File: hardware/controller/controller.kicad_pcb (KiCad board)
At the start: 2 copper layers, 37 x 84 mm, 14 parts, among them J1 Conn_01x02_Pin, J2 Conn_01x02_Pin, J3 Conn_01x02_Pin, J4 Conn_01x02_Pin

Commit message: PCB routing checkpoint 1
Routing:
- net Net-(J1-Pin_2): track 0.00 -> 113.3 mm
- net Net-(J7-Pin_4): track 0.00 -> 75.4 mm
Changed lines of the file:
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@@
 		(layer "Edge.Cuts")
+	)
+	(segment
+		(start 151 62)
+		(end 151 63.5)
+		(width 0.2)
+		(layer "F.Cu")
+		(net 2)
+	)
+	(segment
+		(start 127.525 61.79)
+		(end 127.525 64.975)
+		(width 0.2)
+		(layer "F.Cu")
+		(net 2)
+	)
+	(segment
+		(start 149.525 61.79)
+		(end 147.9075 63.4075)
+		(width 0.2)
+		(layer "F.Cu")
+		(net 2)
+	)
+	(segment
+		(start 126 118.789)
+		(end 126 65)
+		(width 0.2)
+		(layer "F.Cu")
+		(net 2)
+	)
+	(segment
+		(start 127.525 64.975)
+		(end 127.5 65)
+		(width 0.2)
+		(layer "F.Cu")
+		(net 2)
+	)
+	(segment
+		(start 127.5 65)
+		(end 126 65)
+		(width 0.2)
+		(layer "F.Cu")
+		(net 2)
+	)
+	(segment
+		(start 151 63.5)
+		(end 148 63.5)
+		(width 0.2)
+		(layer "F.Cu")
+		(net 2)
+	)
+	(segment
+		(start 141.5 115)
+		(end 139.5 117)
+		(width 0.2)
+		(layer "F.Cu")
+		(net 2)
+	)
+	(segment
+		(start 127.2525 120.0415)
+		(end 126 118.789)
+		(width 0.2)
+		(layer "F.Cu")
+		(net 2)
+	)
+	(segment
+		(start 148 63.5)
+		(end 147.9075 63.4075)
+		(width 0.2)
+		(layer "F.Cu")
+		(net 2)
+	)
+	(segment
+		(start 154.5 61.5)
+		(end 151.5 61.5)
+		(width 0.2)
+		(layer "F.Cu")
+		(net 2)
+	)
+	(segment
+		(start 151.5 61.5)
+		(end 151 62)
+		(width 0.2)
+		(layer "F.Cu")
+		(net 2)
+	)
+	(segment
+		(start 126 65)
+		(end 122.5 61.5)
+		(width 0.2)
+		(layer "F.Cu")
+		(net 2)
+	)
+	(segment
+		(start 139.5 117)
+		(end 130.294 117)
+		(width 0.2)
+		(layer "F.Cu")
+		(net 2)
+	)
+	(segment
+		(start 146.315 65)
+		(end 127.5 65)
+		(width 0.2)
+		(layer "F.Cu")
+		(net 2)
+	)
+	(segment
+		(start 147.9075 63.4075)
+		(end 146.315 65)
+		(width 0.2)
+		(layer "F.Cu")
+		(net 2)
+	)
+	(segment
+		(start 130.294 117)
+		(end 127.2525 120.0415)
+		(width 0.2)
+		(layer "F.Cu")
+		(net 2)
+	)
+	(segment
+		(start 152 128.5)
+		(end 152 119.389)
+		(width 0.2)
+		(layer "F.Cu")
+		(net 12)
+	)
+	(segment
+		(start 137.5 78)
+		(end 137.5 79)
+		(width 0.2)
+		(layer "F.Cu")
+		(net 12)
+	)
+	(segment
+		(start 137.705 102.5)
+		(end 137.705 105.094)
+		(width 0.2)
+		(layer "F.Cu")
+		(net 12)
+	)
+	(segment
+		(start 145.08 76)
+		(end 143.08 78)
+		(width 0.2)
+		(layer "F.Cu")
+		(net 12)
+	)
+	(segment
+		(start 144 128.5)
+		(end 152 128.5)
+		(width 0.2)
+		(layer "F.Cu")
+		(net 12)
+	)
+	(segment
+		(start 137.5 79)
+		(end 137.705 79.205)
+		(width 0.2)
+		(layer "F.Cu")
+		(net 12)
+	)
+	(segment
+		(start 152 119.389)
+		(end 150.1125 117.5015)
+		(width 0.2)
+		(layer "F.Cu")
+		(net 12)
+	)
+	(segment
+		(start 143.08 78)
+		(end 137.5 78)
+		(width 0.2)
+		(layer "F.Cu")
+		(net 12)
+	)
+	(segment
+		(start 137.705 79.205)
+		(end 137.705 102.5)
+		(width 0.2)
+		(layer "F.Cu")
+		(net 12)
+	)
+	(segment
+		(start 137.705 105.094)
+		(end 150.1125 117.5015)
+		(width 0.2)
+		(layer "F.Cu")
+		(net 12)
+	)
+	(segment
+		(start 142.25 130.25)
+		(end 144 128.5)
+		(width 0.2)
+		(layer "F.Cu")
+		(net 12)
 	)
 	(embedded_fonts no)

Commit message: routing checkpoint 2
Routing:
- net Net-(J5-Pin_5): track 0.00 -> 65.1 mm
- net Net-(U1-5V0): track 0.00 -> 61.9 mm
- net Net-(J1-Pin_2): track 113.3 -> 136.2 mm
- net Net-(J7-Pin_4): track 75.4 -> 74.4 mm
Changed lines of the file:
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@@
 	)
 	(segment
-		(start 151 62)
-		(end 151 63.5)
-		(width 0.2)
-		(layer "F.Cu")
-		(net 2)
-	)
-	(segment
-		(start 127.525 61.79)
-		(end 127.525 64.975)
-		(width 0.2)
-		(layer "F.Cu")
-		(net 2)
-	)
-	(segment
-		(start 149.525 61.79)
-		(end 147.9075 63.4075)
+		(start 154.5 61.5)
+		(end 152 59)
 		(width 0.2)
 		(layer "F.Cu")
@@
 	)
 	(segment
-		(start 127.525 64.975)
-		(end 127.5 65)
-		(width 0.2)
-		(layer "F.Cu")
-		(net 2)
-	)
-	(segment
-		(start 127.5 65)
+		(start 127.525 63.475)
 		(end 126 65)
 		(width 0.2)
@@
 	)
 	(segment
-		(start 151 63.5)
-		(end 148 63.5)
+		(start 127.525 61.79)
+		(end 127.525 63.475)
 		(width 0.2)
 		(layer "F.Cu")
@@
 	)
 	(segment
+		(start 126 53.5)
+		(end 147 53.5)
+		(width 0.2)
+		(layer "F.Cu")
+		(net 2)
+	)
+	(segment
+		(start 149.525 61.79)
+		(end 147 59.265)
+		(width 0.2)
+		(layer "F.Cu")
+		(net 2)
+	)
+	(segment
+		(start 125 64)
+		(end 125 54.5)
+		(width 0.2)
+		(layer "F.Cu")
+		(net 2)
+	)
+	(segment
+		(start 152 59)
+		(end 152 53.5)
+		(width 0.2)
+		(layer "F.Cu")
+		(net 2)
+	)
+	(segment
+		(start 125 54.5)
+		(end 126 53.5)
+		(width 0.2)
+		(layer "F.Cu")
+		(net 2)
+	)
+	(segment
+		(start 125 64)
+		(end 122.5 61.5)
+		(width 0.2)
+		(layer "F.Cu")
+		(net 2)
+	)
+	(segment
 		(start 127.2525 120.0415)
 		(end 126 118.789)
@@
 	)
 	(segment
-		(start 148 63.5)
-		(end 147.9075 63.4075)
-		(width 0.2)
-		(layer "F.Cu")
-		(net 2)
-	)
-	(segment
-		(start 154.5 61.5)
-		(end 151.5 61.5)
-		(width 0.2)
-		(layer "F.Cu")
-		(net 2)
-	)
-	(segment
-		(start 151.5 61.5)
-		(end 151 62)
-		(width 0.2)
-		(layer "F.Cu")
-		(net 2)
-	)
-	(segment
-		(start 126 65)
-		(end 122.5 61.5)
+		(start 152 53.5)
+		(end 147 53.5)
+		(width 0.2)
+		(layer "F.Cu")
+		(net 2)
+	)
+	(segment
+		(start 147 59.265)
+		(end 147 53.5)
 		(width 0.2)
 		(layer "F.Cu")
@@
 	)
 	(segment
-		(start 146.315 65)
-		(end 127.5 65)
-		(width 0.2)
-		(layer "F.Cu")
-		(net 2)
-	)
-	(segment
-		(start 147.9075 63.4075)
-		(end 146.315 65)
+		(start 149.525 61.975)
+		(end 149.525 61.79)
+		(width 0.2)
+		(layer "F.Cu")
+		(net 2)
+	)
+	(segment
+		(start 126 65)
+		(end 125 64)
 		(width 0.2)
 		(layer "F.Cu")
@@
 	)
 	(segment
+		(start 134.5 65.2195)
+		(end 134.5 65)
+		(width 0.2)
+		(layer "F.Cu")
+		(net 9)
+	)
+	(segment
+		(start 138.5 65)
+		(end 138.5 58.41)
+		(width 0.2)
+		(layer "F.Cu")
+		(net 9)
+	)
+	(segment
+		(start 128.7195 109.8395)
+		(end 128.7195 71)
+		(width 0.2)
+		(layer "F.Cu")
+		(net 9)
+	)
+	(segment
+		(start 133.88 115)
+		(end 128.7195 109.8395)
+		(width 0.2)
+		(layer "F.Cu")
+		(net 9)
+	)
+	(segment
+		(start 134.5 65)
+		(end 138.5 65)
+		(width 0.2)
+		(layer "F.Cu")
+		(net 9)
+	)
+	(segment
+		(start 128.7195 71)
+		(end 134.5 65.2195)
+		(width 0.2)
+		(layer "F.Cu")
+		(net 9)
+	)
+	(segment
+		(start 138.41 78.5)
+		(end 137.705 79.205)
+		(width 0.2)
+		(layer "F.Cu")
+		(net 12)
+	)
+	(segment
 		(start 152 128.5)
 		(end 152 119.389)
@@
 	)
 	(segment
-		(start 137.5 78)
-		(end 137.5 79)
-		(width 0.2)
-		(layer "F.Cu")
-		(net 12)
-	)
-	(segment
 		(start 137.705 102.5)
 		(end 137.705 105.094)
@@
 	)
 	(segment
+		(start 137.705 79.205)
+		(end 137.705 102.5)
+		(width 0.2)
+		(layer "F.Cu")
+		(net 12)
+	)
+	(segment
+		(start 144 128.5)
+		(end 152 128.5)
+		(width 0.2)
+		(layer "F.Cu")
+		(net 12)
+	)
+	(segment
+		(start 152 119.389)
+		(end 150.1125 117.5015)
+		(width 0.2)
+		(layer "F.Cu")
+		(net 12)
+	)
+	(segment
 		(start 145.08 76)
 		(end 143.08 78)
@@
 	)
 	(segment
-		(start 144 128.5)
-		(end 152 128.5)
-		(width 0.2)
-		(layer "F.Cu")
-		(net 12)
-	)
-	(segment
-		(start 137.5 79)
-		(end 137.705 79.205)
-		(width 0.2)
-		(layer "F.Cu")
-		(net 12)
-	)
-	(segment
-		(start 152 119.389)
-		(end 150.1125 117.5015)
-		(width 0.2)
-		(layer "F.Cu")
-		(net 12)
-	)
-	(segment
-		(start 143.08 78)
-		(end 137.5 78)
-		(width 0.2)
-		(layer "F.Cu")
-		(net 12)
-	)
-	(segment
-		(start 137.705 79.205)
-		(end 137.705 102.5)
+		(start 138.5 78.5)
+		(end 138.41 78.5)
 		(width 0.2)
 		(layer "F.Cu")
@@
 	)
 	(segment
+		(start 143.08 78)
+		(end 139 78)
+		(width 0.2)
+		(layer "F.Cu")
+		(net 12)
+	)
+	(segment
 		(start 142.25 130.25)
 		(end 144 128.5)
@@
 		(net 12)
 	)
+	(segment
+		(start 139 78)
+		(end 138.5 78.5)
+		(width 0.2)
+		(layer "F.Cu")
+		(net 12)
+	)
+	(segment
+		(start 127.2525 117.5015)
+		(end 128.3185 116.4355)
+		(width 0.2)
+		(layer "F.Cu")
+		(net 24)
+	)
+	(segment
+		(start 134 65)
+		(end 133.9 64.9)
+		(width 0.2)
+		(layer "F.Cu")
+		(net 24)
+	)
+	(segment
+		(start 128.3185 70.6815)
+		(end 134 65)
+		(width 0.2)
+		(layer "F.Cu")
+		(net 24)
+	)
+	(segment
+		(start 128.3185 116.4355)
+		(end 128.3185 70.6815)
+		(width 0.2)
+		(layer "F.Cu")
+		(net 24)
+	)
+	(segment
+		(start 133.9 64.9)
+		(end 133.9 58.41)
+		(width 0.2)
+		(layer "F.Cu")
+		(net 24)
+	)
 	(embedded_fonts no)

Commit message: routing done
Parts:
- Listener Switch1: renamed from Listener Switch
- Power Switch1: renamed from Power Switch
- USB C Lipo1: renamed from USB C Lipo
- moved J1 6.43 mm to (127.5, 63.0), turned to 180 degrees
- moved J2 5.90 mm to (123.0, 63.0), turned to 180 degrees
- moved R4 5.06 mm to (150.5, 133.0), turned to 180 degrees
- moved J4 4.07 mm to (154.0, 63.0), turned to 180 degrees
- moved J3 3.75 mm to (149.5, 63.0), turned to 180 degrees
- moved R2 3.54 mm to (127.5, 130.0)
- moved R1 3.05 mm to (127.5, 133.0)
- moved UWB1 1.01 mm to (145.2, 75.0)
- renumbered IMU to IMU1, UWB to UWB1
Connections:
- ESP32 pad J1_1: Net-(U1-3V3) -> Net-(ESP32-3V3)
- IMU1 pad 6: Net-(J7-Pin_6) -> Net-(ESP32-3V3)
- R1 pad 2: Net-(U1-3V3) -> Net-(ESP32-3V3)
- R2 pad 2: Net-(U1-3V3) -> Net-(ESP32-3V3)
- R3 pad 1: Net-(U1-3V3) -> Net-(ESP32-3V3)
- R4 pad 2: Net-(U1-3V3) -> Net-(ESP32-3V3)
- UWB1 pad 6: Net-(J7-Pin_6) -> Net-(ESP32-3V3)
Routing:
- net Net-(ESP32-GPIO17): track 0.00 -> 110.3 mm
- net Net-(ESP32-GPIO15): track 0.00 -> 100.4 mm
- net Net-(ESP32-3V3): track 0.00 -> 87.4 mm
- net Net-(ESP32-GPIO2): track 0.00 -> 78.0 mm
- net Net-(ESP32-GPIO4): track 0.00 -> 74.0 mm
- net Net-(ESP32-GPIO6): track 0.00 -> 69.7 mm
- net Net-(ESP32-GND3): track 136.2 -> 112.2 mm
- net Net-(ESP32-U0TXD/GPIO43): track 0.00 -> 14.9 mm
- net Net-(ESP32-GPIO21): track 0.00 -> 12.9 mm
- net Net-(ESP32-5V0): track 61.9 -> 74.5 mm
- net Net-(ESP32-U0RXD/GPIO44): track 0.00 -> 11.3 mm
- net Net-(ESP32-RST): track 0.00 -> 9.12 mm
- net Net-(ESP32-GPIO1): track 0.00 -> 8.37 mm
- net Net-(ESP32-GPIO48): track 0.00 -> 8.28 mm
- net Net-(ESP32-GND1): track 74.4 -> 67.1 mm
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
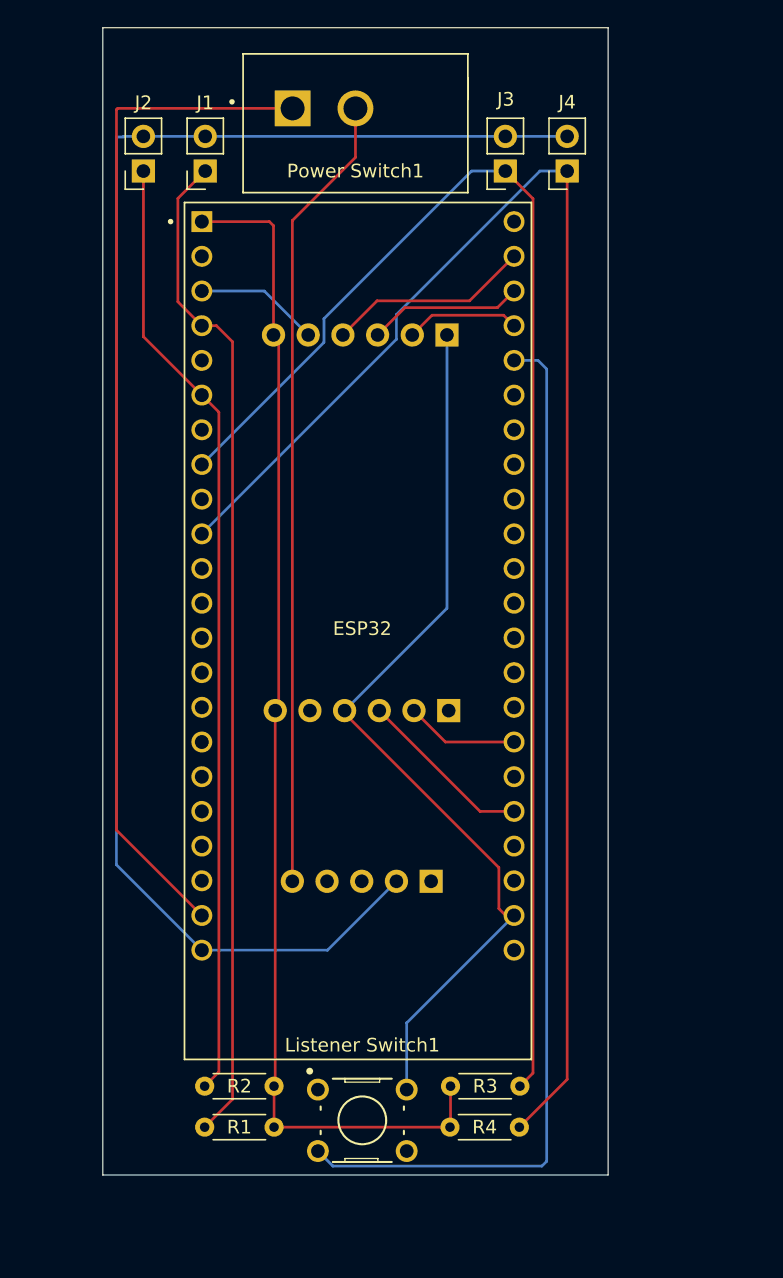
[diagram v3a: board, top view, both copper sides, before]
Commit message: routing and screw hole placement done
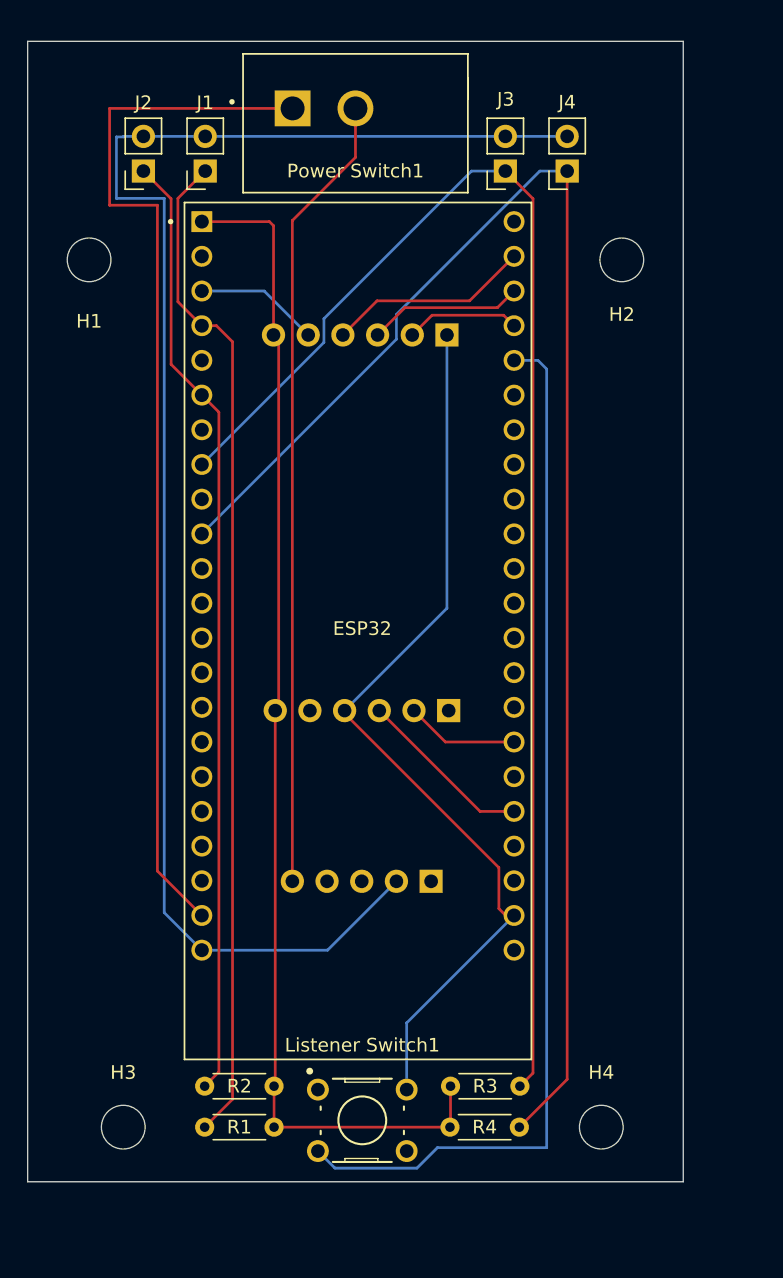
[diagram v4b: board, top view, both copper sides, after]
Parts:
- added H1: MountingHole, MountingHole:MountingHole_3.2mm_M3, F.Cu at (119.0, 69.5)
- added H2: MountingHole, MountingHole:MountingHole_3.2mm_M3, F.Cu at (158.0, 69.5)
- added H3: MountingHole, MountingHole:MountingHole_3.2mm_M3, F.Cu at (121.5, 133.0)
- added H4: MountingHole, MountingHole:MountingHole_3.2mm_M3, F.Cu at (156.5, 133.0)
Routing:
- net Net-(ESP32-5V0): track 74.5 -> 77.3 mm
- net Net-(ESP32-GND3): track 112.2 -> 114.3 mm
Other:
- board size 37 x 84 mm -> 48 x 83.5 mm

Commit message: edits made, PCB ready for 1st run
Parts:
- moved Power Switch1 75.6 mm to (138.5, 135.1)
- moved Listener Switch1 71.5 mm to (138.8, 61.0)
- moved H1 11.5 mm to (119.0, 58.0)
- moved H2 11.0 mm to (158.0, 58.5)
- moved R3 8.78 mm to (149.0, 138.0), turned to 90 degrees
- moved H3 5.15 mm to (119.0, 137.5)
- moved H4 4.74 mm to (158.0, 137.5)
- moved J2 4.55 mm to (127.5, 62.5)
- moved J1 4.03 mm to (131.5, 62.5)
- moved J4 4.03 mm to (150.0, 62.5)
- moved R2 3.55 mm to (125.5, 133.0), turned to -90 degrees
- moved J3 3.54 mm to (146.0, 62.5)
- moved R4 1.00 mm to (151.5, 133.0), turned to -90 degrees
- moved R1 0.54 mm to (128.0, 133.0), turned to -90 degrees
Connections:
- ESP32 pad J1_3: Net-(ESP32-RST) -> unconnected-(ESP32-RST-PadJ1_3)
- ESP32 pad J3_6: unconnected-(ESP32-MTMS/GPIO42-PadJ3_6) -> Net-(ESP32-MTMS/GPIO42)
- Listener Switch1 pad 3: Net-(ESP32-GPIO2) -> Net-(ESP32-MTMS/GPIO42)
- UWB1 pad 2: Net-(ESP32-GPIO1) -> Net-(ESP32-GPIO2)
- UWB1 pad 3: Net-(ESP32-U0RXD/GPIO44) -> Net-(ESP32-GPIO1)
- UWB1 pad 4: Net-(ESP32-U0TXD/GPIO43) -> Net-(ESP32-U0RXD/GPIO44)
- UWB1 pad 5: Net-(ESP32-RST) -> Net-(ESP32-U0TXD/GPIO43)
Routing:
- net Net-(ESP32-GPIO2): track 77.5 -> 8.22 mm
- net Net-(ESP32-5V0): track 77.3 -> 19.3 mm
- net Net-(USB C Lipo1-Pin_5): track 58.5 -> 20.9 mm
- net Net-(ESP32-MTMS/GPIO42): track 0.00 -> 32.2 mm
- net Net-(ESP32-GPIO17): track 110.3 -> 90.4 mm
- net Net-(ESP32-3V3): track 87.4 -> 104.8 mm
- net Net-(ESP32-GND1): track 67.1 -> 82.6 mm
- net Net-(ESP32-GPIO15): track 100.4 -> 90.0 mm
- net Net-(ESP32-RST): track 9.12 -> 0.00 mm
- net Net-(ESP32-GND3): track 114.3 -> 108.8 mm
- net Net-(ESP32-GPIO4): track 74.0 -> 79.1 mm
- net Net-(ESP32-GPIO6): track 69.7 -> 73.8 mm
- net Net-(ESP32-U0TXD/GPIO43): track 14.9 -> 17.5 mm
- net Net-(ESP32-U0RXD/GPIO44): track 11.3 -> 13.9 mm
- net Net-(ESP32-GPIO1): track 8.37 -> 10.9 mm
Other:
- board size 48 x 83.5 mm -> 48 x 88.5 mm

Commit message: added fab files
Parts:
- removed Listener Switch1: B3F-1000, B3F_1000:SW_B3F-1000
- removed Power Switch1: GF-123-0054, GF_123_0054:SW_GF-123-0054
- added Listener Switch: B3F-1000, Omron Tactile Button Small B3f-1000:SW_B3F-1000, F.Cu at (138.8, 61.0)
- added Power Switch: GF-123-0054, On/Off Switch:SW_GF-123-0054, F.Cu at (138.5, 135.5)
- added Project F.A.L.C.O.N.: LOGO, LOGO, F.Cu at (118.8, 96.7)
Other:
- board text added: "SDP Team 1 - 2026"
